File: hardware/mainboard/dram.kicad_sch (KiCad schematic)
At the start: 16 parts

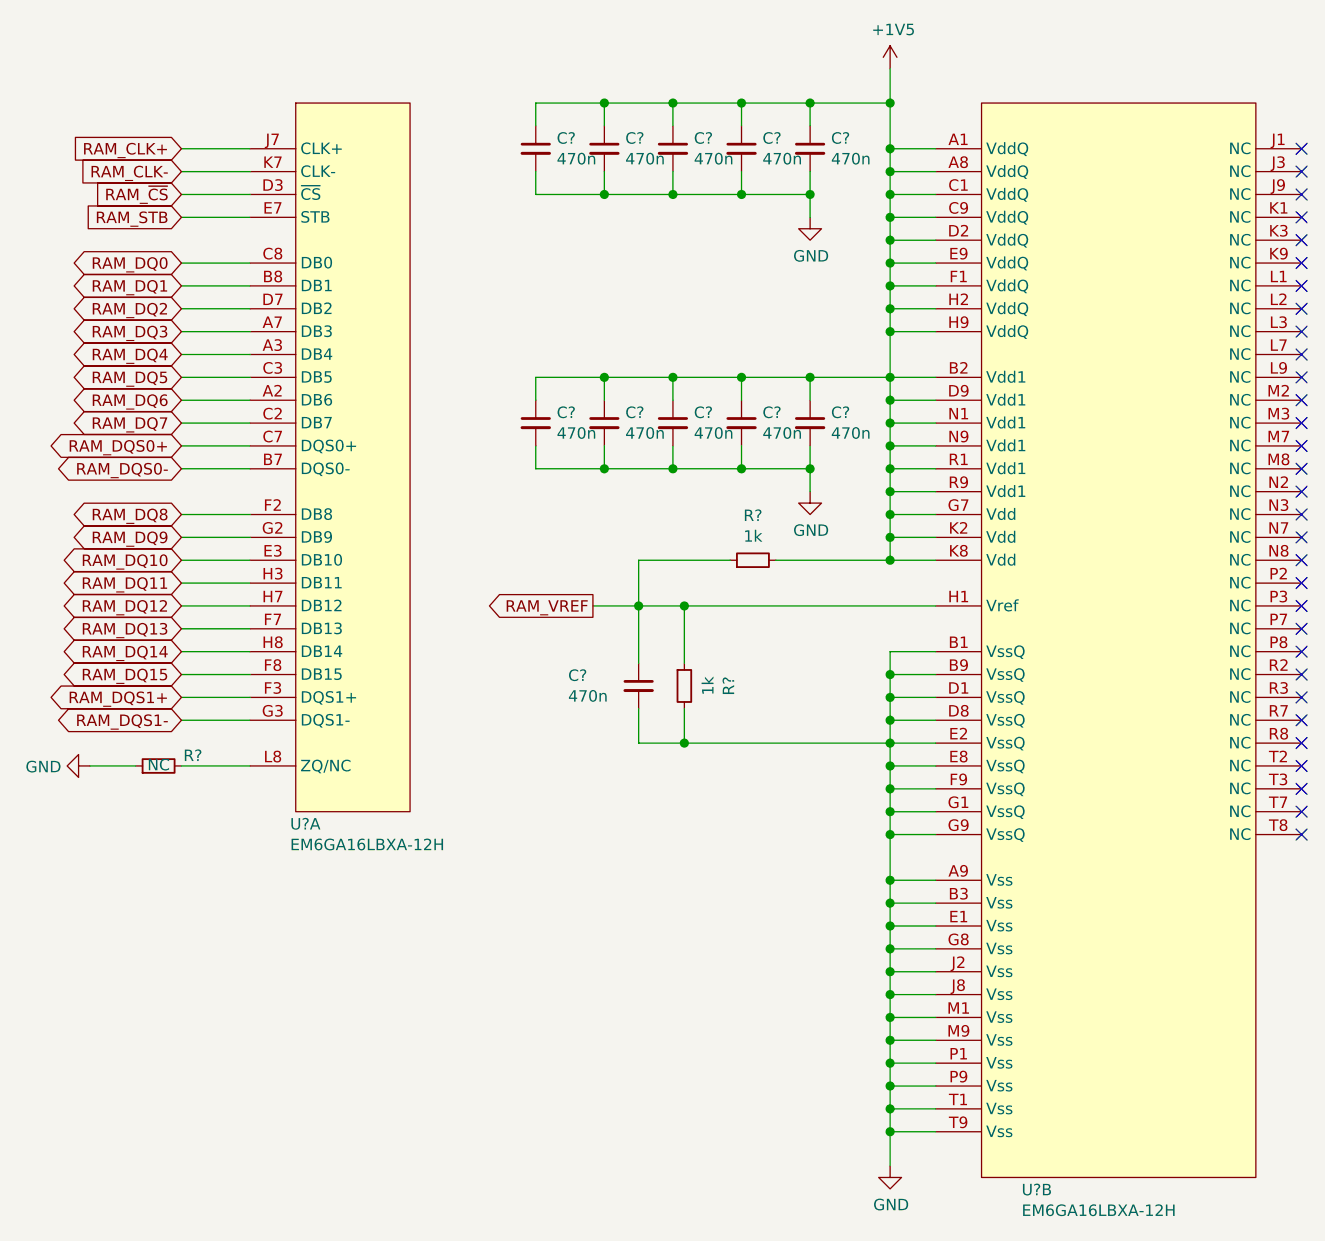
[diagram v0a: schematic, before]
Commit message: Annotate and assign some footpints
Signed-off-by: David Shah <dave@ds0.me>
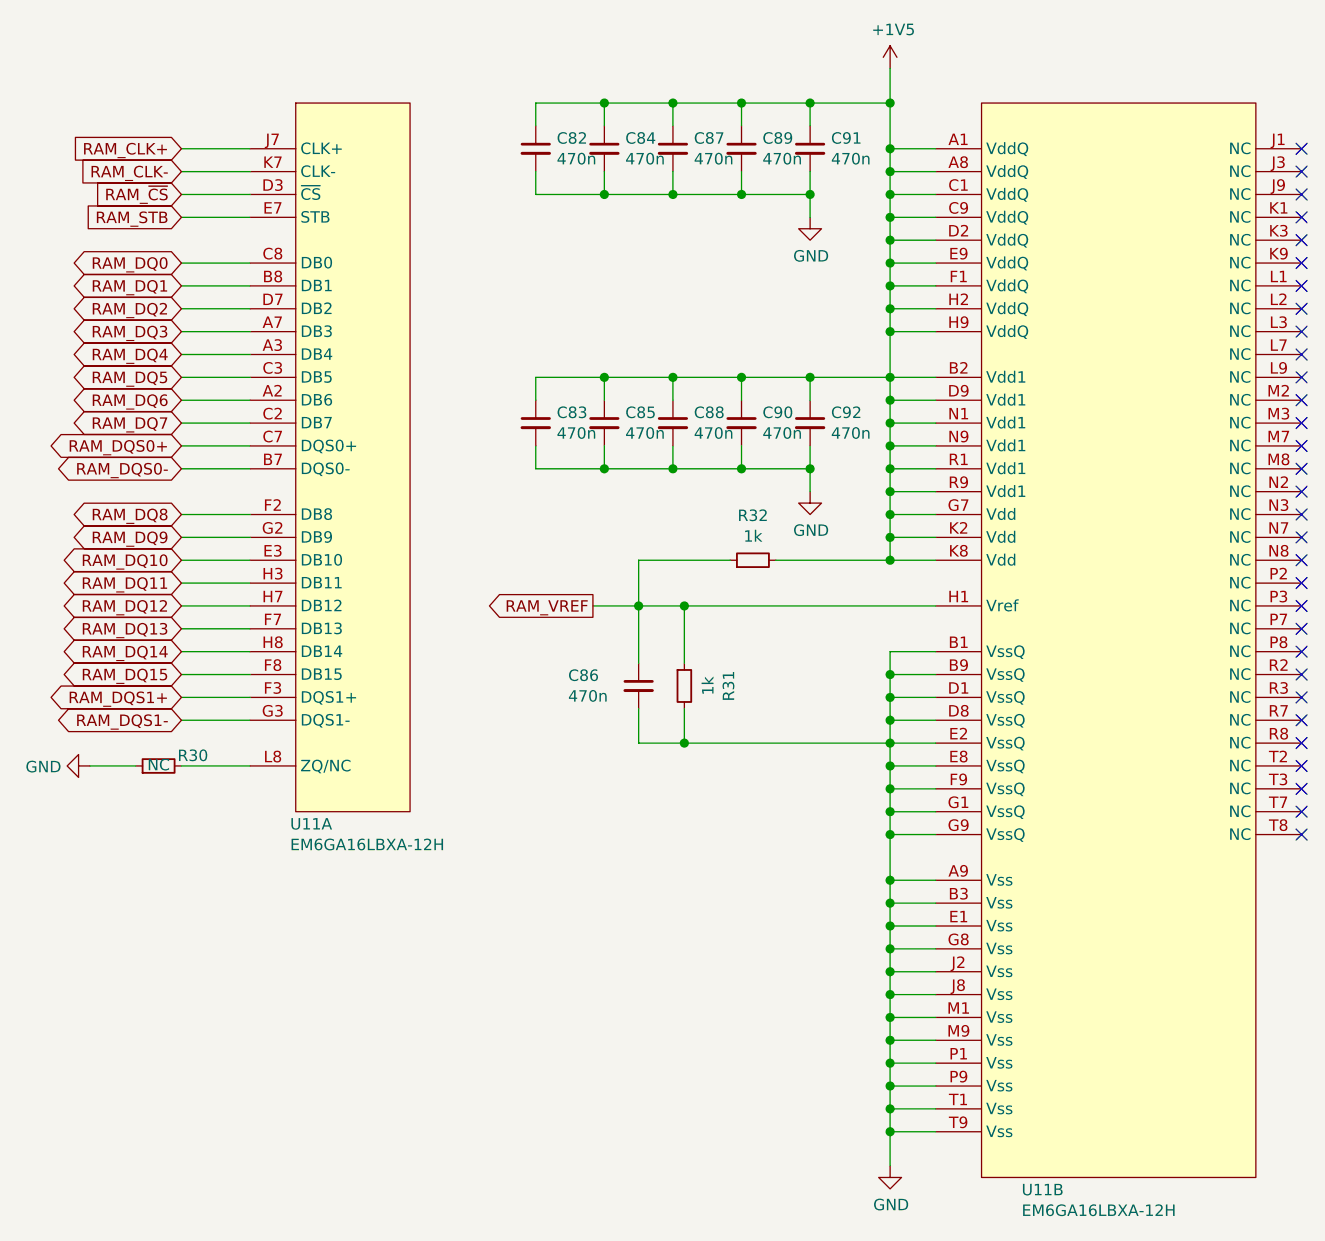
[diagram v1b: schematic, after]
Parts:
- C82, C83, C84, C85, C86, C87, C88, C89, C90, C91, C92: renamed from C?; footprint (none) -> Capacitor_SMD:C_0402_1005Metric
- R30, R31, R32: renamed from R?; footprint (none) -> Resistor_SMD:R_0402_1005Metric
- U11: renamed from U?; footprint (none) -> Package_BGA:BGA-96_9.0x13.0mm_Layout2x3x16_P0.8mm

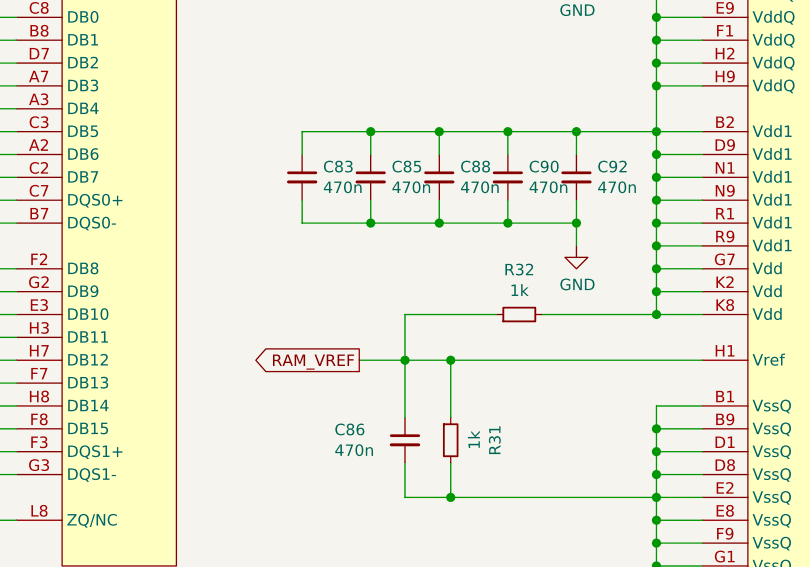
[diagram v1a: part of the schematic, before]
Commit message: mainboard: Fix some schematic ERC issues
Signed-off-by: gatecat <gatecat@ds0.me>
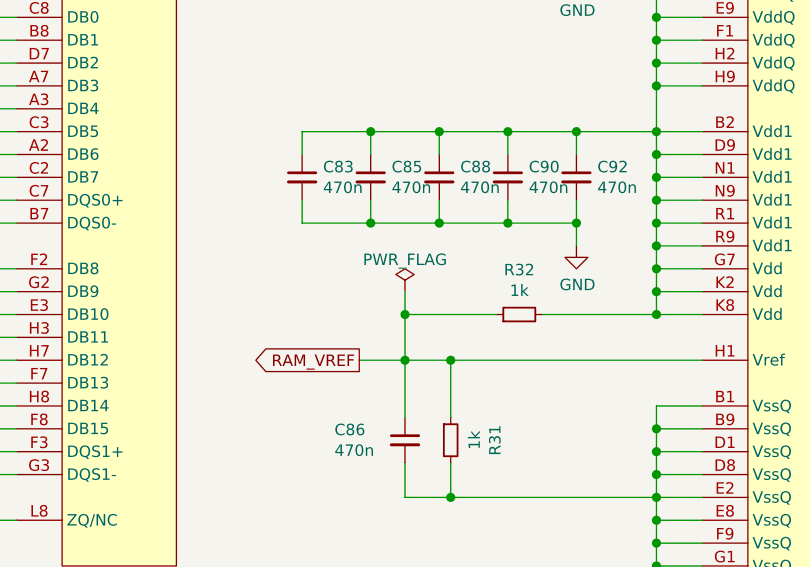
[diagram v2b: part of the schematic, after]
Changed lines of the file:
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@@
   (junction (at 148.59 55.88) (diameter 1.016) (color 0 0 0 0))
   (junction (at 148.59 66.04) (diameter 1.016) (color 0 0 0 0))
+  (junction (at 152.4 76.2) (diameter 1.016) (color 0 0 0 0))
   (junction (at 152.4 81.28) (diameter 1.016) (color 0 0 0 0))
   (junction (at 156.21 25.4) (diameter 1.016) (color 0 0 0 0))
@@
     (stroke (width 0) (type solid) (color 0 0 0 0))
   )
+  (wire (pts (xy 152.4 73.66) (xy 152.4 76.2))
+    (stroke (width 0) (type solid) (color 0 0 0 0))
+  )
   (wire (pts (xy 152.4 76.2) (xy 152.4 81.28))
     (stroke (width 0) (type solid) (color 0 0 0 0))
@@
     )
     (property "Datasheet" "" (id 3) (at 180.34 21.59 0)
+      (effects (font (size 1.27 1.27)) hide)
+    )
+    (pin "1")
+  )
+  (symbol (lib_id "power:PWR_FLAG") (at 152.4 73.66 0) (unit 1)
+    (in_bom yes) (on_board yes)
+    (property "Reference" "#FLG0113" (id 0) (at 152.4 71.755 0)
+      (effects (font (size 1.27 1.27)) hide)
+    )
+    (property "Value" "PWR_FLAG" (id 1) (at 152.4 70.1126 0))
+    (property "Footprint" "" (id 2) (at 152.4 73.66 0)
+      (effects (font (size 1.27 1.27)) hide)
+    )
+    (property "Datasheet" "~" (id 3) (at 152.4 73.66 0)
       (effects (font (size 1.27 1.27)) hide)
     )
@@
       (effects (font (size 1.27 1.27)) hide)
     )
+    (pin "A2")
+    (pin "A3")
+    (pin "A7")
+    (pin "B7")
+    (pin "B8")
+    (pin "C2")
+    (pin "C3")
+    (pin "C7")
+    (pin "C8")
+    (pin "D3")
+    (pin "D7")
+    (pin "E3")
+    (pin "E7")
+    (pin "F2")
+    (pin "F3")
+    (pin "F7")
+    (pin "F8")
+    (pin "G2")
+    (pin "G3")
+    (pin "H3")
+    (pin "H7")
+    (pin "H8")
     (pin "J7")
     (pin "K7")
-    (pin "D3")
-    (pin "E7")
-    (pin "C8")
-    (pin "B8")
-    (pin "D7")
-    (pin "A7")
-    (pin "A3")
-    (pin "C3")
-    (pin "A2")
-    (pin "C2")
-    (pin "C7")
-    (pin "B7")
-    (pin "F2")
-    (pin "G2")
-    (pin "E3")
-    (pin "H3")
-    (pin "H7")
-    (pin "F7")
-    (pin "H8")
-    (pin "F8")
-    (pin "F3")
-    (pin "G3")
     (pin "L8")
   )
@@
     (pin "A1")
     (pin "A8")
+    (pin "A9")
+    (pin "B1")
+    (pin "B2")
+    (pin "B3")
+    (pin "B9")
     (pin "C1")
     (pin "C9")
+    (pin "D1")
     (pin "D2")
+    (pin "D8")
+    (pin "D9")
+    (pin "E1")
+    (pin "E2")
+    (pin "E8")
     (pin "E9")
     (pin "F1")
+    (pin "F9")
+    (pin "G1")
+    (pin "G7")
+    (pin "G8")
+    (pin "G9")
+    (pin "H1")
     (pin "H2")
     (pin "H9")
-    (pin "H1")
-    (pin "B2")
-    (pin "D9")
-    (pin "N1")
-    (pin "N9")
-    (pin "R1")
-    (pin "R9")
-    (pin "G7")
-    (pin "K2")
-    (pin "K8")
-    (pin "B1")
-    (pin "B9")
-    (pin "D1")
-    (pin "D8")
-    (pin "E2")
-    (pin "E8")
-    (pin "F9")
-    (pin "G1")
-    (pin "G9")
-    (pin "A9")
-    (pin "B3")
-    (pin "E1")
-    (pin "G8")
+    (pin "J1")
     (pin "J2")
+    (pin "J3")
     (pin "J8")
-    (pin "M1")
-    (pin "M9")
-    (pin "P1")
-    (pin "P9")
-    (pin "T1")
-    (pin "T9")
-    (pin "J1")
-    (pin "J3")
     (pin "J9")
     (pin "K1")
+    (pin "K2")
     (pin "K3")
+    (pin "K8")
     (pin "K9")
     (pin "L1")
@@
     (pin "L7")
     (pin "L9")
+    (pin "M1")
     (pin "M2")
     (pin "M3")
     (pin "M7")
     (pin "M8")
+    (pin "M9")
+    (pin "N1")
     (pin "N2")
     (pin "N3")
     (pin "N7")
     (pin "N8")
+    (pin "N9")
+    (pin "P1")
     (pin "P2")
     (pin "P3")
     (pin "P7")
     (pin "P8")
+    (pin "P9")
+    (pin "R1")
     (pin "R2")
     (pin "R3")
     (pin "R7")
     (pin "R8")
+    (pin "R9")
+    (pin "T1")
     (pin "T2")
     (pin "T3")
     (pin "T7")
     (pin "T8")
+    (pin "T9")
   )
 )
